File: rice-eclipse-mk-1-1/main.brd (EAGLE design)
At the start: 110.2 x 91.2 mm, 106 parts, among them IC1 LMV321LICTRT, IC2 LMV321LICTRT, IC3 LMV321LICTRT, IC4 LMV321LICTRT, IC5 UA78M, IC6 LMV321LICTRT, U1 LM1084ISX-5.0/NOPB, U2 THS4531IDRD8-M, U3 THS4531IDRD8-M, U4 THS4531IDRD8-M, U5 THS4531IDRD8-M, U6 1101M2S3CQE2, X1 2540-5

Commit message: Added some stuff.
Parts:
- moved X6 0.25 mm to (99.6, 40.9)
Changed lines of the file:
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@@
 <element name="R25" library="rcl" library_urn="urn:adsk.eagle:library:334" package="R0603" package3d_urn="urn:adsk.eagle:package:23555/2" value="500K" x="59.436" y="81.28" rot="R180"/>
 <element name="X5" library="con-phoenix-250-extra" package="1770908" value="" x="99.568" y="77.978" rot="R270"/>
-<element name="X6" library="con-phoenix-250-extra" package="1770908" value="" x="99.822" y="40.894" rot="R270"/>
+<element name="X6" library="con-phoenix-250-extra" package="1770908" value="" x="99.568" y="40.894" rot="R270"/>
 <element name="U6" library="SLIDE_SW" package="1101M2S3CQE2" value="1101M2S3CQE2" x="26.67" y="2.794">
 <attribute name="COPYRIGHT" value="Copyright (C) 2015 Accelerated Designs. All rights reserved" x="26.67" y="2.794" size="1.778" layer="27" display="off"/>
@@
 <contactref element="X6" pad="P$8"/>
 <contactref element="X6" pad="P$4"/>
-<wire x1="102.522" y1="29.844" x2="107.522" y2="29.844" width="0" layer="19" extent="1-1"/>
-<wire x1="106.172" y1="21.844" x2="107.522" y2="29.844" width="0" layer="19" extent="1-1"/>
+<wire x1="102.268" y1="29.844" x2="107.268" y2="29.844" width="0" layer="19" extent="1-1"/>
+<wire x1="106.172" y1="21.844" x2="107.268" y2="29.844" width="0" layer="19" extent="1-1"/>
 </signal>
 <signal name="LC_1_OUT+">
@@
 <contactref element="X6" pad="P$3"/>
 <contactref element="X6" pad="P$7"/>
-<wire x1="102.522" y1="32.344" x2="107.522" y2="32.344" width="0" layer="19" extent="1-1"/>
-<wire x1="103.672" y1="21.844" x2="102.522" y2="32.344" width="0" layer="19" extent="1-1"/>
+<wire x1="102.268" y1="32.344" x2="107.268" y2="32.344" width="0" layer="19" extent="1-1"/>
+<wire x1="103.672" y1="21.844" x2="102.268" y2="32.344" width="0" layer="19" extent="1-1"/>
 </signal>
 <signal name="ADC1_A0">
@@
 <contactref element="X6" pad="P$2"/>
 <contactref element="X6" pad="P$6"/>
-<wire x1="107.522" y1="34.844" x2="105.664" y2="47.244" width="0" layer="19" extent="1-1"/>
-<wire x1="102.522" y1="34.844" x2="107.522" y2="34.844" width="0" layer="19" extent="1-1"/>
+<wire x1="107.268" y1="34.844" x2="105.664" y2="47.244" width="0" layer="19" extent="1-1"/>
+<wire x1="102.268" y1="34.844" x2="107.268" y2="34.844" width="0" layer="19" extent="1-1"/>
 </signal>
 <signal name="LC_2_OUT+">
@@
 <contactref element="X6" pad="P$5"/>
 <contactref element="X6" pad="P$1"/>
-<wire x1="102.522" y1="37.344" x2="103.164" y2="47.244" width="0" layer="19" extent="1-1"/>
-<wire x1="107.522" y1="37.344" x2="102.522" y2="37.344" width="0" layer="19" extent="1-1"/>
+<wire x1="102.268" y1="37.344" x2="103.164" y2="47.244" width="0" layer="19" extent="1-1"/>
+<wire x1="107.268" y1="37.344" x2="102.268" y2="37.344" width="0" layer="19" extent="1-1"/>
 </signal>
 <signal name="ADC1_A2">

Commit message: Board is ready to route.
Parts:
- added C21, C24, C27: 10nF, rcl:C0603
- added C22, C23, C25, C26, C28, C29: (no value), rcl:C025-025X050
- added IC7, IC8, IC9: LMV321LICTRT, st-microelectronics-extra:SOT23-5
- added R42, R43, R44, R45, R46, R47, R48, R49, R50, R51, R52, R53, R54, R56, R57, R58, R59: ?, rcl:0204/7
- added R55: 10, rcl:R0603
- R32, R33: value 150 -> 10
- R34: value 150 -> ?; device rcl:R0603 -> rcl:0204/7
- moved C19 16.3 mm to (50.8, 40.4), turned to 0 degrees
- moved C20 14.1 mm to (51.8, 43.7), turned to 0 degrees
- moved R40 12.9 mm to (46.5, 44.5), turned to 270 degrees
- moved IC6 10.5 mm to (53.8, 47.2)
- moved C18 10.2 mm to (50.0, 47.2)
- moved X8 8.92 mm to (49.0, 53.1)
- moved JP3 8.54 mm to (91.2, 35.6)
- moved ADC3 7.44 mm to (46.2, 59.9)
- moved X3 7.38 mm to (90.9, 10.7)
- moved C2 7.13 mm to (42.2, 68.1)
- moved R41 6.84 mm to (46.2, 34.8), turned to 270 degrees
- moved R37 6.55 mm to (48.8, 26.9), turned to 0 degrees
- moved R30 6.37 mm to (48.8, 67.1)
- moved R34 6.12 mm to (70.4, 17.8), turned to 270 degrees
- moved IC4 5.61 mm to (82.0, 22.4)
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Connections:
- new net N$26: IC2.3, R42.1, R43.2
- new net N$27: IC2.1, R44.2, R45.1
- new net N$28: C22.1, R46.1, R47.2
- new net N$29: C23.1, IC7.1, R47.1
- new net N$30: C25.1, R48.1, R49.2
- new net N$31: C26.1, IC8.1, R49.1
- new net N$32: C28.1, R50.1, R51.2
- new net N$33: C29.1, IC9.1, R51.1
- new net N$34: IC3.3, R34.1, R52.2
- new net N$35: IC3.1, R53.2, R54.1
- new net N$36: IC4.3, R56.1, R57.2
- new net N$37: IC4.1, R58.2, R59.1
- new net PT2_PREC: IC2.4, R43.1, R46.2
- new net PT3_PREC: IC3.4, R48.2, R52.1
- new net PT4_PREC: IC4.4, R50.2, R57.1
- net +3V3_PT: now also C21.1, C24.1, C27.1, IC7.5, IC8.5, IC9.5, R44.1, R53.1, R58.1
- net ADC2_A1: now also IC7.3, IC7.4; no longer IC2.3, IC2.4
- net ADC2_A2: now also IC8.3, IC8.4; no longer IC3.3, IC3.4
- net ADC2_A3: now also IC9.3, IC9.4; no longer IC4.3, IC4.4
- net GND: now also C21.2, C22.2, C23.2, C24.2, C25.2, C26.2, C27.2, C28.2, C29.2, IC7.2, IC8.2, IC9.2, R45.2, R54.2, R55.1, R59.2; no longer R34.1
- net PT2_VS-: now also R42.2; no longer IC2.1
- net PT3_VS-: now also R34.2; no longer IC3.1
- net PT4_VS-: now also R55.2, R56.2; no longer IC4.1, R34.2

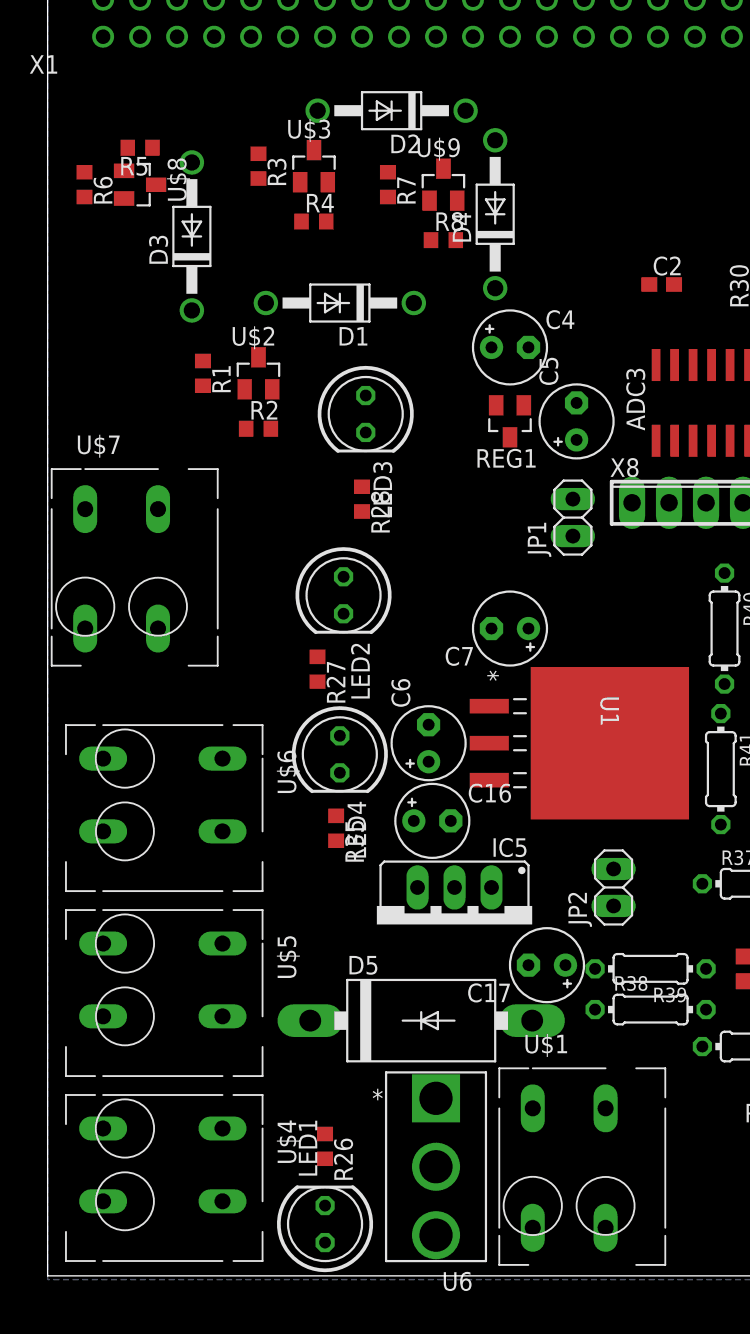
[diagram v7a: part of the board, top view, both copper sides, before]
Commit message: Routed power traces. Autorouter starts next.
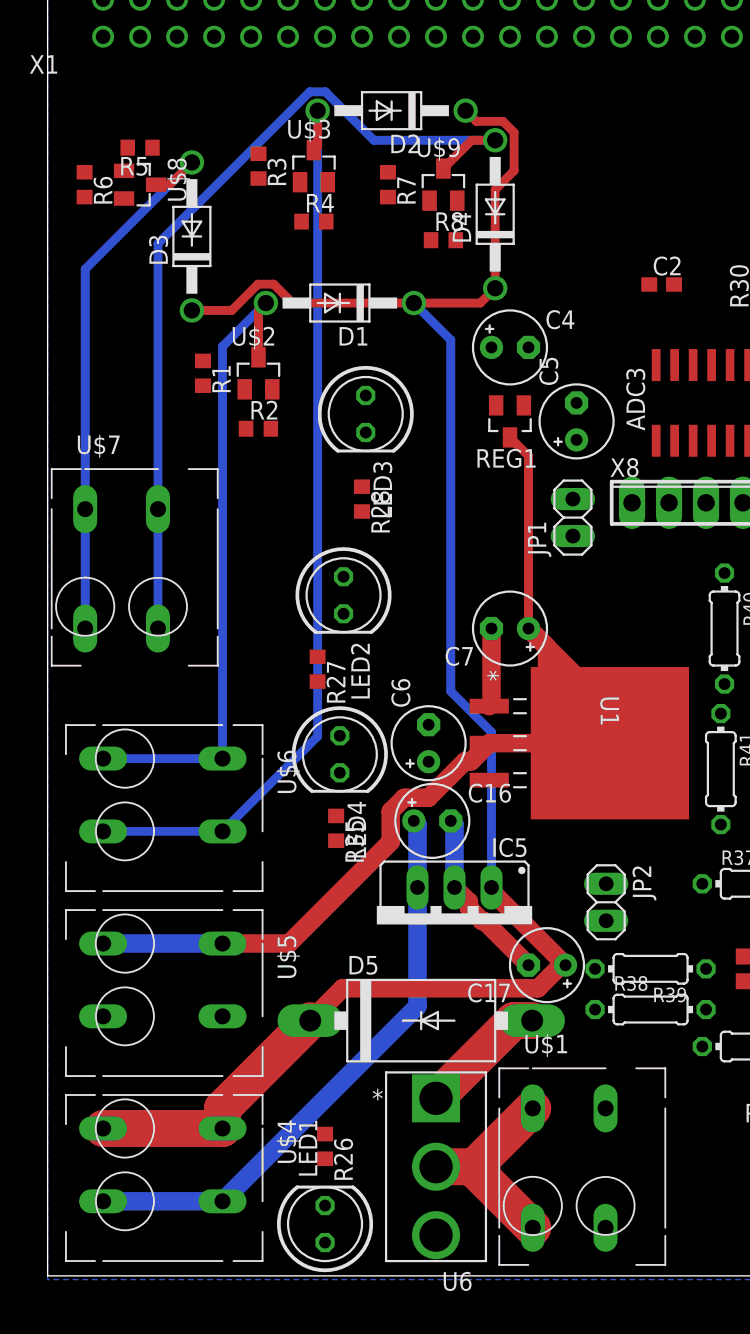
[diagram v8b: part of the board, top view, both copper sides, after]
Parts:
- moved JP2 1.14 mm to (38.4, 25.7), turned to 270 degrees
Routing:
- net +12V: track 0.00 -> 124.7 mm
- net +5V: track 0.00 -> 69.1 mm
- net SOLENOID_1_NEGATIVE: track 0.00 -> 63.2 mm
- net SOLENOID_3_NEGATIVE: track 0.00 -> 59.6 mm
- net RELAY_NEGATIVE: track 0.00 -> 44.7 mm
- net +10V: track 0.00 -> 40.0 mm
- net SOLENOID_2_NEGATIVE: track 0.00 -> 38.6 mm
- net GND: track 0.00 -> 17.6 mm
- net +12V_DEBUG: track 0.00 -> 14.2 mm
- net N$4: track 0.00 -> 8.81 mm
